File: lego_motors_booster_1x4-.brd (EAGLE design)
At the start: 40.6 x 65.4 mm, 21 parts, among them Q1 IRF4905, Q3 BS170T, Q5 BUZ11BV, X1 NXT-SOCKET, X2 NXT-SOCKET, X3 NXT-SOCKET, X4 NXT-SOCKET, X5 NXT-SOCKET

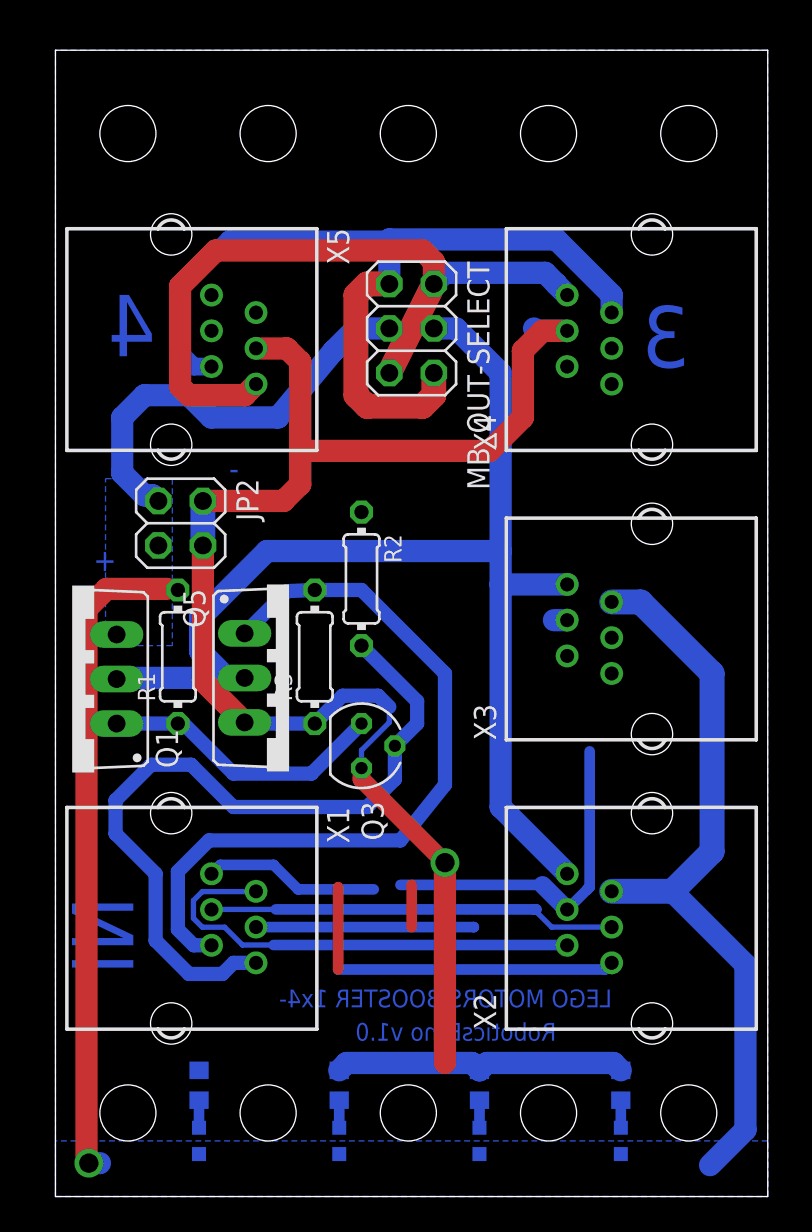
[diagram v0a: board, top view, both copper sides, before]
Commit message: lego_motors_booster_1x4-: second version with different layout => all other things same
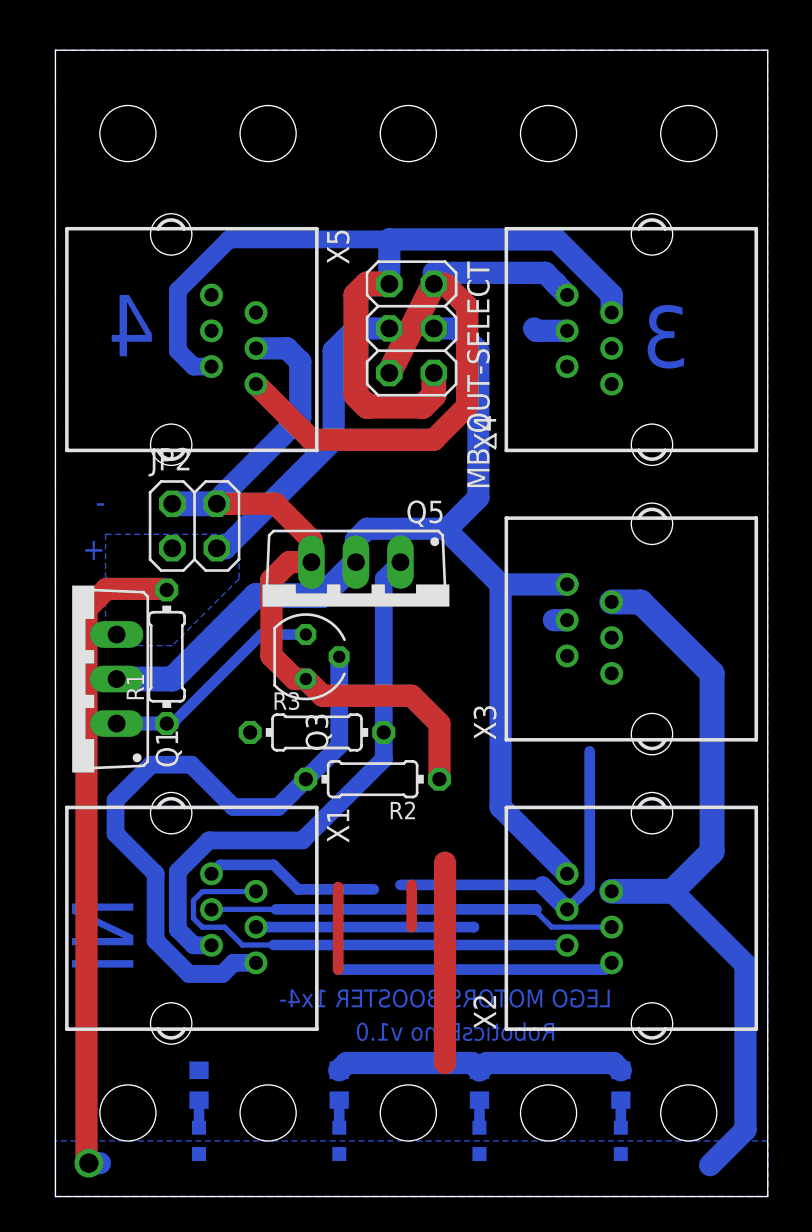
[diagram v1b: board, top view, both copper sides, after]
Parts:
- moved R2 11.4 mm to (18.1, 22.5), turned to 180 degrees
- moved Q3 5.99 mm to (14.3, 29.5)
- moved Q5 5.57 mm to (17.1, 32.4), turned to 180 degrees
- moved R3 4.32 mm to (14.9, 25.2), turned to 0 degrees
- moved JP2 0.81 mm to (7.94, 37.0), turned to 0 degrees
- moved R1 0.64 mm to (6.35, 29.5)
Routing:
- net GND: track 133.4 -> 106.7 mm, vias 1 -> 0
- net MA1: track 43.9 -> 31.6 mm
- net MA0: track 43.6 -> 36.9 mm
- net VCC: track 104.3 -> 97.8 mm
- net MA0_OUT: track 70.0 -> 63.5 mm
- net MB0_OUT: track 41.5 -> 36.8 mm
- net N$1: track 16.3 -> 12.9 mm

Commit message: mirrored + maybe some minor improvements
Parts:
- moved X2 40.0 mm to (0.00, 15.9), flipped to the bottom
- moved X3 40.0 mm to (0.00, 32.4), flipped to the bottom
- moved X4 40.0 mm to (0.00, 48.9), flipped to the bottom
- moved X1 38.8 mm to (39.4, 15.9), flipped to the bottom
- moved X5 38.8 mm to (39.4, 48.9), flipped to the bottom
- moved Q1 38.1 mm to (39.0, 29.5), flipped to the bottom
- moved R1 27.3 mm to (33.6, 30.8), flipped to the bottom
- moved LED4 24.5 mm to (7.74, 3.17), flipped to the top
- moved R7 24.5 mm to (7.74, 6.35), flipped to the top
- moved JP2 24.2 mm to (32.1, 38.3), flipped to the bottom
- moved LED1 23.7 mm to (31.8, 3.17), flipped to the top
- moved R4 23.7 mm to (31.8, 6.35), flipped to the top
- moved Q3 11.5 mm to (25.7, 30.8), flipped to the bottom
- moved R3 10.2 mm to (25.1, 26.5), flipped to the bottom
- moved LED3 8.48 mm to (15.8, 3.17), flipped to the top
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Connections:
- removed net N$11: X4.4
- removed net N$12: X4.5
- removed net N$13: X4.6
- removed net N$17: X5.4
- removed net N$18: X5.5
- removed net N$19: X5.6
- removed net N$5: X3.4
- removed net N$6: X3.5
- removed net N$7: X3.6
- net GND: no longer X3.3, X4.3, X5.3
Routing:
- net GND: track 106.7 -> 91.4 mm
- added copper zone on layer 1, net GND
- added copper zone on layer 1, net VCC
- removed copper zone on layer 16, net GND
- removed copper zone on layer 16, net VCC
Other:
- board size 40.6 x 65.4 mm -> 40 x 65 mm
- board text added: "RoboticsBrno v1.1"
- board text removed: "RoboticsBrno v1.0"
